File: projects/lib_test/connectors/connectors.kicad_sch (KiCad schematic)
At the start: 29 parts, among them X1001 1x02_PH, X1002 1x02_VH, X1003 1x02_PH, X1004 1x06_PH, X1005 1x07_PH, X1006 1x08_PH, X1007 1x06, X1008 1x10, X1009 2x03, X1010 1x15, X1011 2p_5.08, X1012 socket_male, X1013 3p_5.08, X1014 1x03_PH, X1015 1x03_PH, X1016 1x04_PH, X1017 1x04_VH, X1018 1x04_PH, X1019 din41612_plug, X1020 din41612_receptacle, X1021 din41612_receptacle, X1022 dc_005, X1023 sub_d_hd_plug, X1024 sub_d_hd_receptacle, X1025 usb_c, X1026 usb_b, X1027 SMA, X1028 RCJ6A-H, X1029 TC2030-IDC

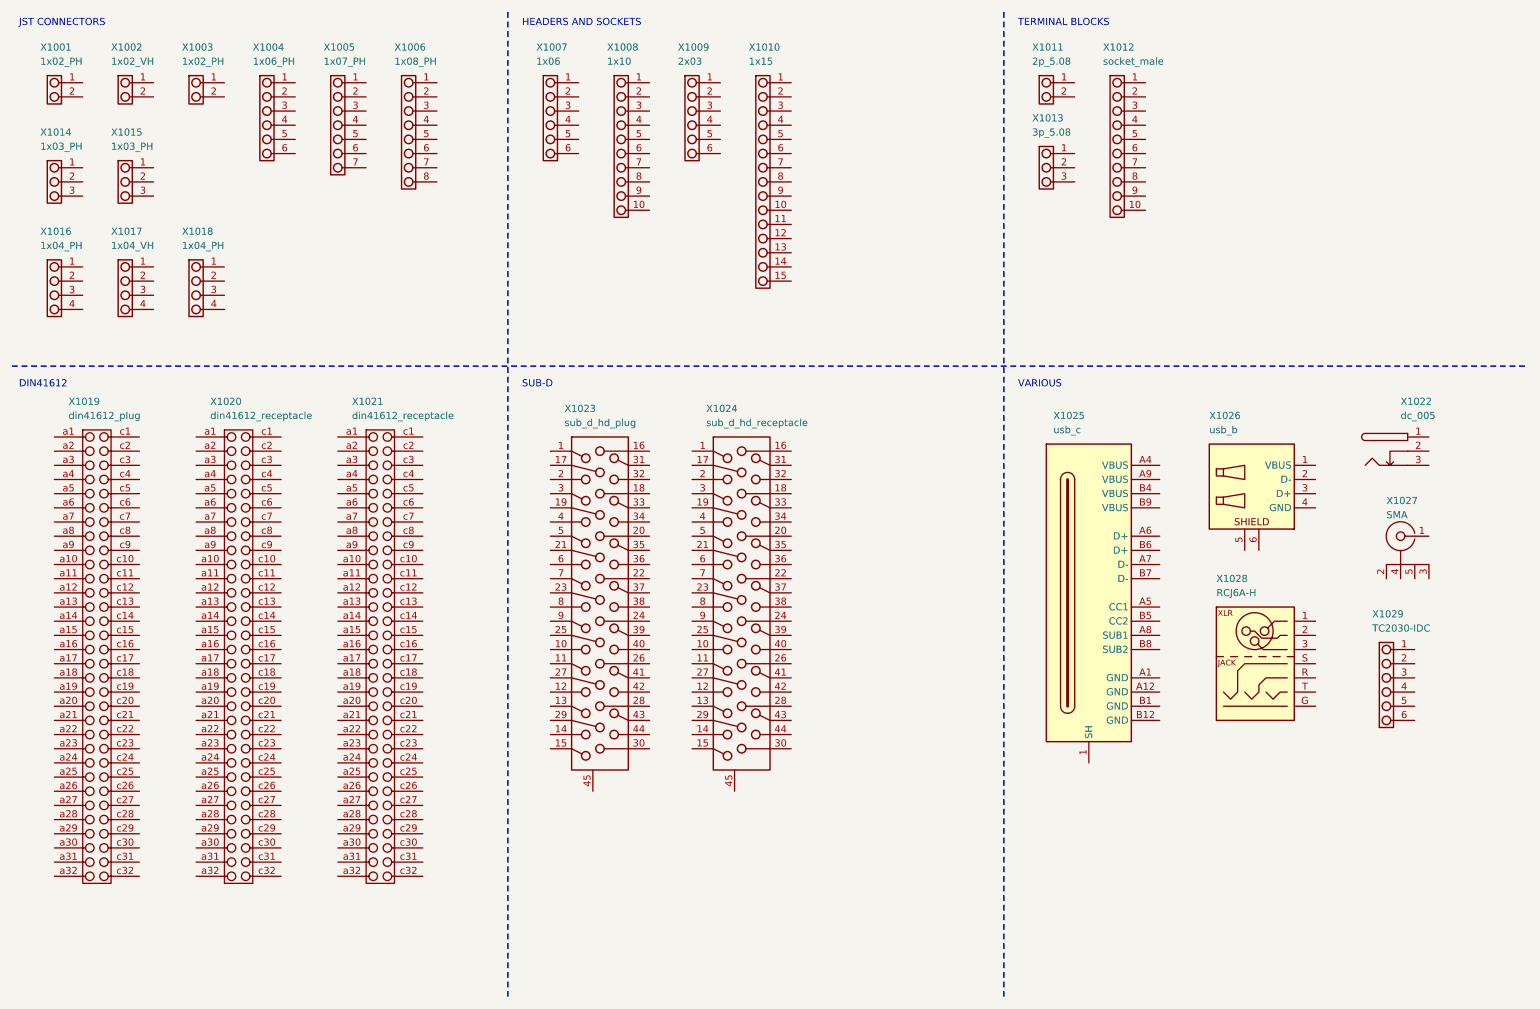
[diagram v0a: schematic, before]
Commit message: add header 2 pin 5.08mm pitch
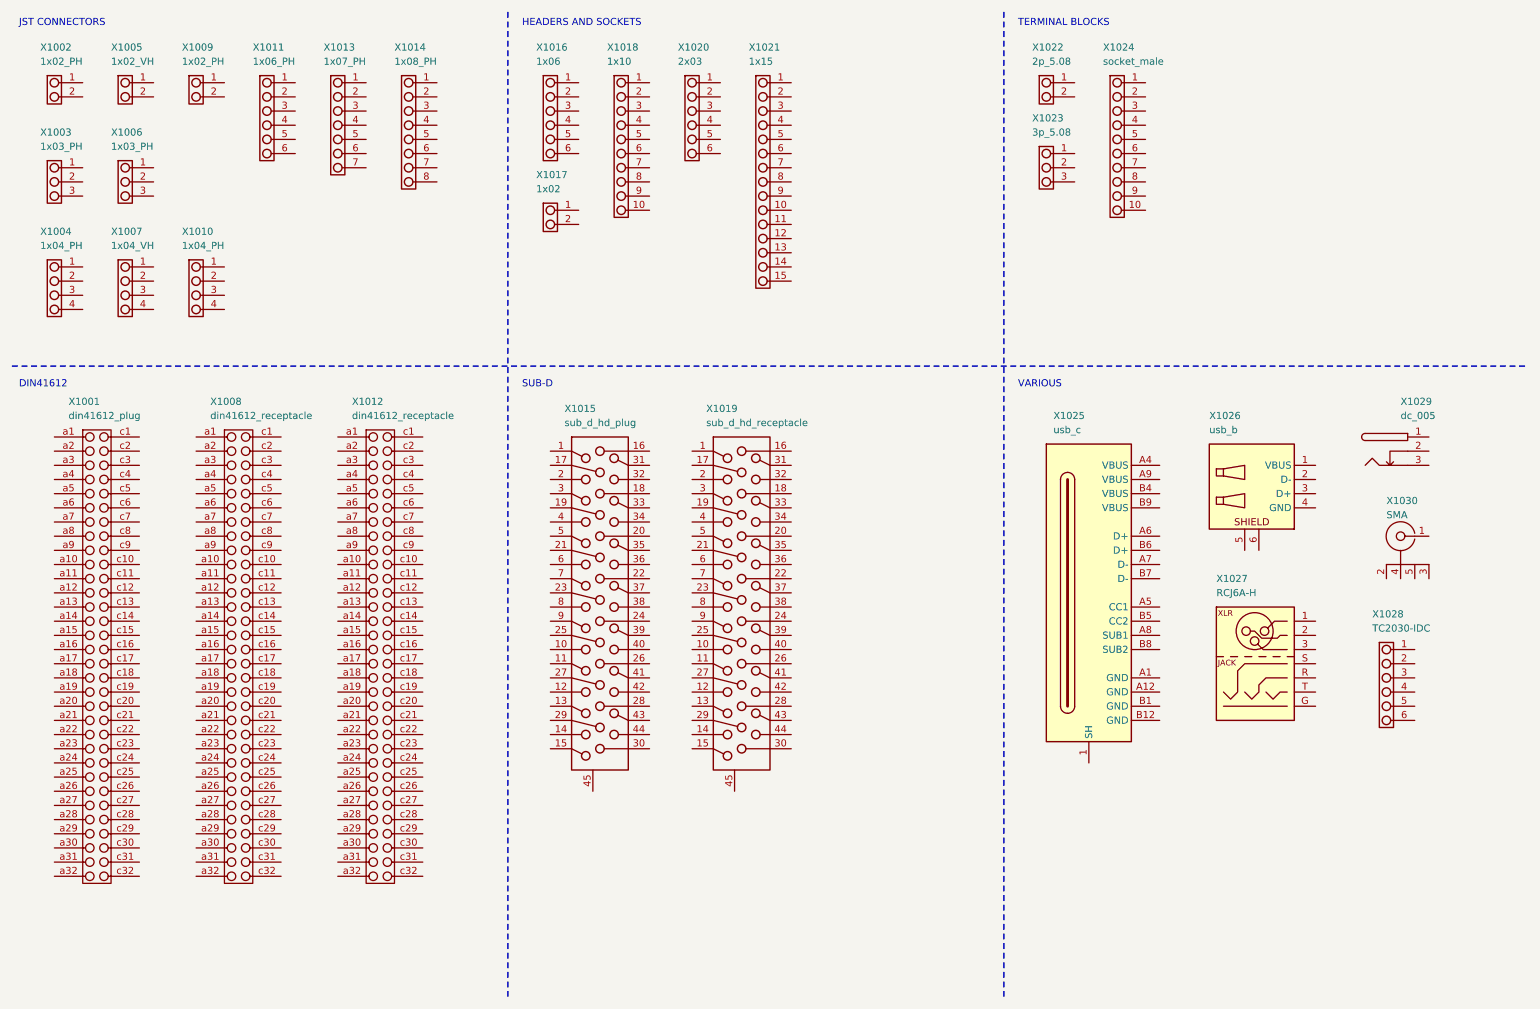
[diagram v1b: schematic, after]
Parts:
- added X1017: 1x02, lily_footprints:con_header_1x02_5.08mm_th, symbol lily_symbols:con_header_1x02_5.08mm_th
- renumbered X1019 to X1001, X1001 to X1002, X1014 to X1003, X1016 to X1004, X1002 to X1005, X1015 to X1006, X1017 to X1007, X1020 to X1008, X1003 to X1009, X1018 to X1010, X1004 to X1011, X1021 to X1012, X1005 to X1013, X1006 to X1014, X1023 to X1015, X1007 to X1016, X1008 to X1018, X1024 to X1019, X1009 to X1020, X1010 to X1021, X1011 to X1022, X1013 to X1023, X1012 to X1024, X1028 to X1027, X1029 to X1028, X1022 to X1029, X1027 to X1030

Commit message: add jumper to project
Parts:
- added X1031: 1x02, lily_footprints:con_header_1x02_2.54mm_th, symbol lily_symbols:con_jumper_1x02_2.54mm_th
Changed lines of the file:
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@@
 			)
 		)
-		(property "Datasheet" "https://lilytronics.github.io/lily_kicad_lib/datasheets/multicomp/2211S-10G.pdf"
+		(property "Datasheet" "https://lilytronics.github.io/lily_kicad_lib/datasheets/multicomp/2211S-MC347.pdf"
 			(at 121.92 71.12 0)
 			(hide yes)
@@
 					(unit 1)
 				)
+			)
+		)
+	)
+	(symbol
+		(lib_id "lily_symbols:con_jumper_1x02_2.54mm_th")
+		(at 165.1 25.4 0)
+		(unit 1)
+		(body_style 1)
+		(exclude_from_sim no)
+		(in_bom yes)
+		(on_board yes)
+		(in_pos_files no)
+		(dnp no)
+		(property "Reference" "X1031"
+			(at 167.64 19.05 0)
+			(show_name no)
+			(do_not_autoplace no)
+			(effects
+				(font
+					(size 1.27 1.27)
+				)
+				(justify left)
+			)
+		)
+		(property "Value" "1x02"
+			(at 167.64 21.59 0)
+			(show_name no)
+			(do_not_autoplace no)
+			(effects
+				(font
+					(size 1.27 1.27)
+				)
+				(justify left)
+			)
+		)
+		(property "Footprint" "lily_footprints:con_header_1x02_2.54mm_th"
+			(at 168.91 33.02 0)
+			(hide yes)
+			(show_name no)
+			(do_not_autoplace no)
+			(effects
+				(font
+					(size 1.27 1.27)
+				)
+			)
+		)
+		(property "Datasheet" "https://lilytronics.github.io/lily_kicad_lib/datasheets/multicomp/2211S-MC347.pdf"
+			(at 170.18 45.72 0)
+			(hide yes)
+			(show_name no)
+			(do_not_autoplace no)
+			(effects
+				(font
+					(size 1.27 1.27)
+				)
+			)
+		)
+		(property "Description" ""
+			(at 165.1 25.4 0)
+			(hide yes)
+			(show_name no)
+			(do_not_autoplace no)
+			(effects
+				(font
+					(size 1.27 1.27)
+				)
+			)
+		)
+		(property "Revision" "1"
+			(at 170.18 27.94 0)
+			(hide yes)
+			(show_name no)
+			(do_not_autoplace no)
+			(effects
+				(font
+					(size 1.27 1.27)
+				)
+			)
+		)
+		(property "Status" "Active"
+			(at 170.18 30.48 0)
+			(hide yes)
+			(show_name no)
+			(do_not_autoplace no)
+			(effects
+				(font
+					(size 1.27 1.27)
+				)
+			)
+		)
+		(property "Manufacturer" "Multicomp"
+			(at 170.18 35.56 0)
+			(hide yes)
+			(show_name no)
+			(do_not_autoplace no)
+			(effects
+				(font
+					(size 1.27 1.27)
+				)
+			)
+		)
+		(property "Manufacturer_ID" "2211S-02G"
+			(at 170.18 38.1 0)
+			(hide yes)
+			(show_name no)
+			(do_not_autoplace no)
+			(effects
+				(font
+					(size 1.27 1.27)
+				)
+			)
+		)
+		(property "Lily_ID" "NO_ID"
+			(at 170.18 40.64 0)
+			(hide yes)
+			(show_name no)
+			(do_not_autoplace no)
+			(effects
+				(font
+					(size 1.27 1.27)
+				)
+			)
+		)
+		(property "JLCPCB_ID" "NO_ID"
+			(at 170.18 43.18 0)
+			(hide yes)
+			(show_name no)
+			(do_not_autoplace no)
+			(effects
+				(font
+					(size 1.27 1.27)
+				)
+			)
+		)
+		(pin "2"
+		)
+		(pin "1"
+		)
+		(instances
+			(project "connectors"
+				(path "/e63e39d7-6ac0-4ffd-8aa3-1841a4541b55"
+					(reference "X1031")
+					(unit 1)
+				)
